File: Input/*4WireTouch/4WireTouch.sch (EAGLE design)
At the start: 15 parts, among them U2 DRV8834RGET

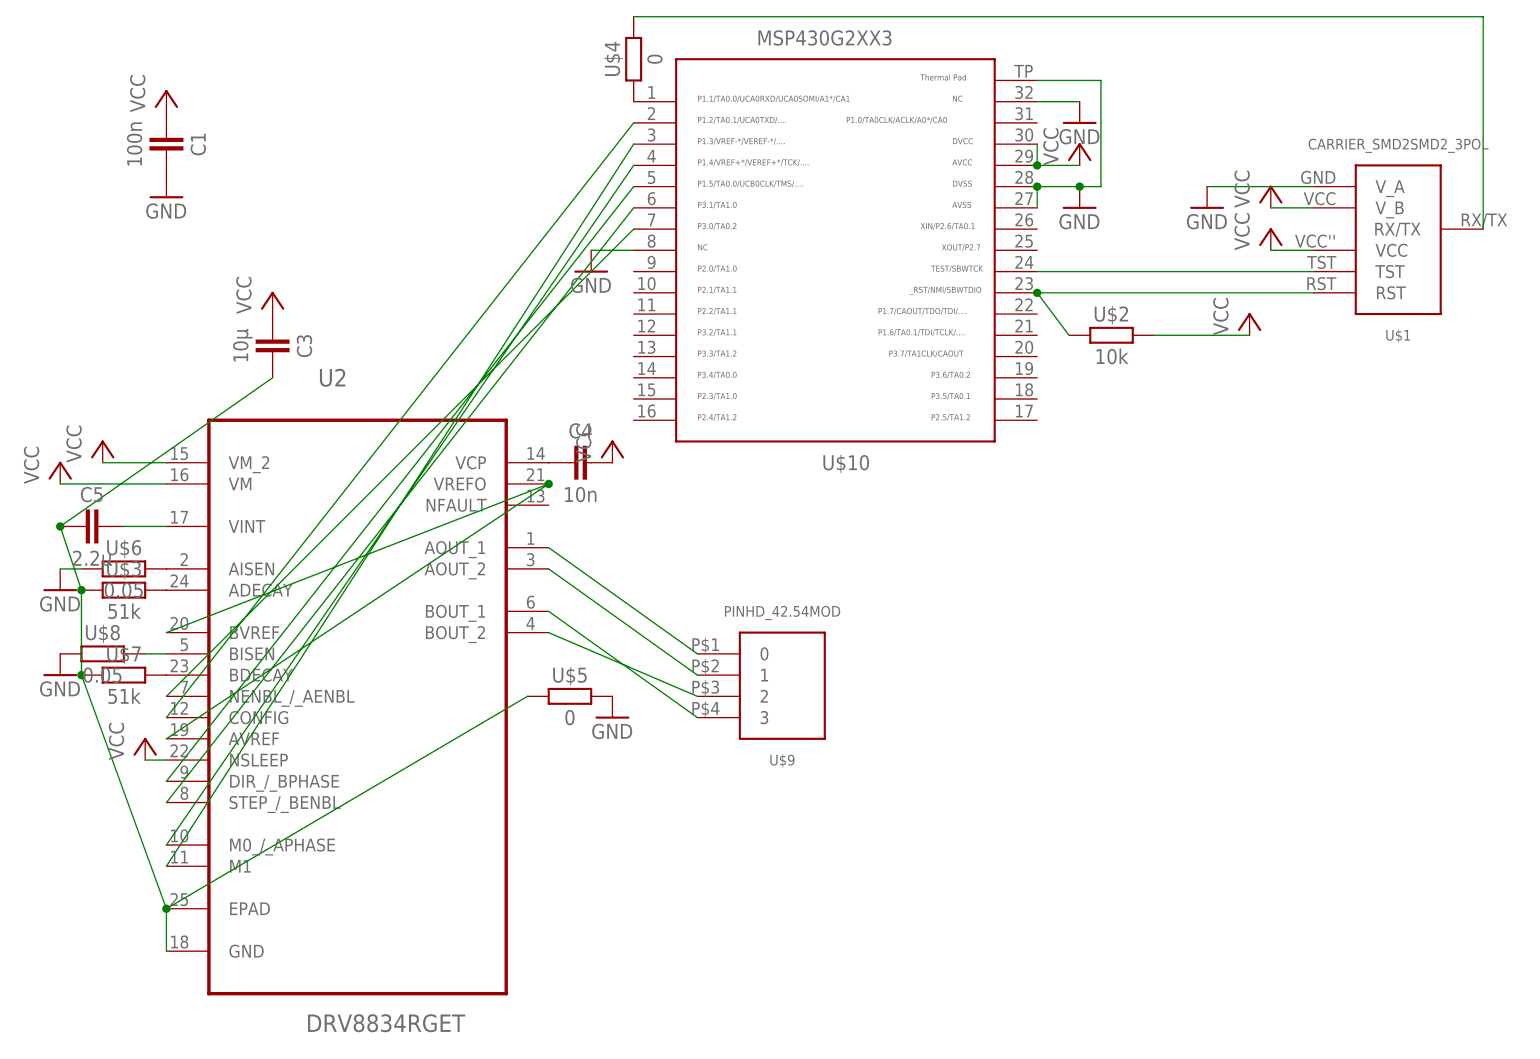
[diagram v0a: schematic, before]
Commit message: Update Pinheader
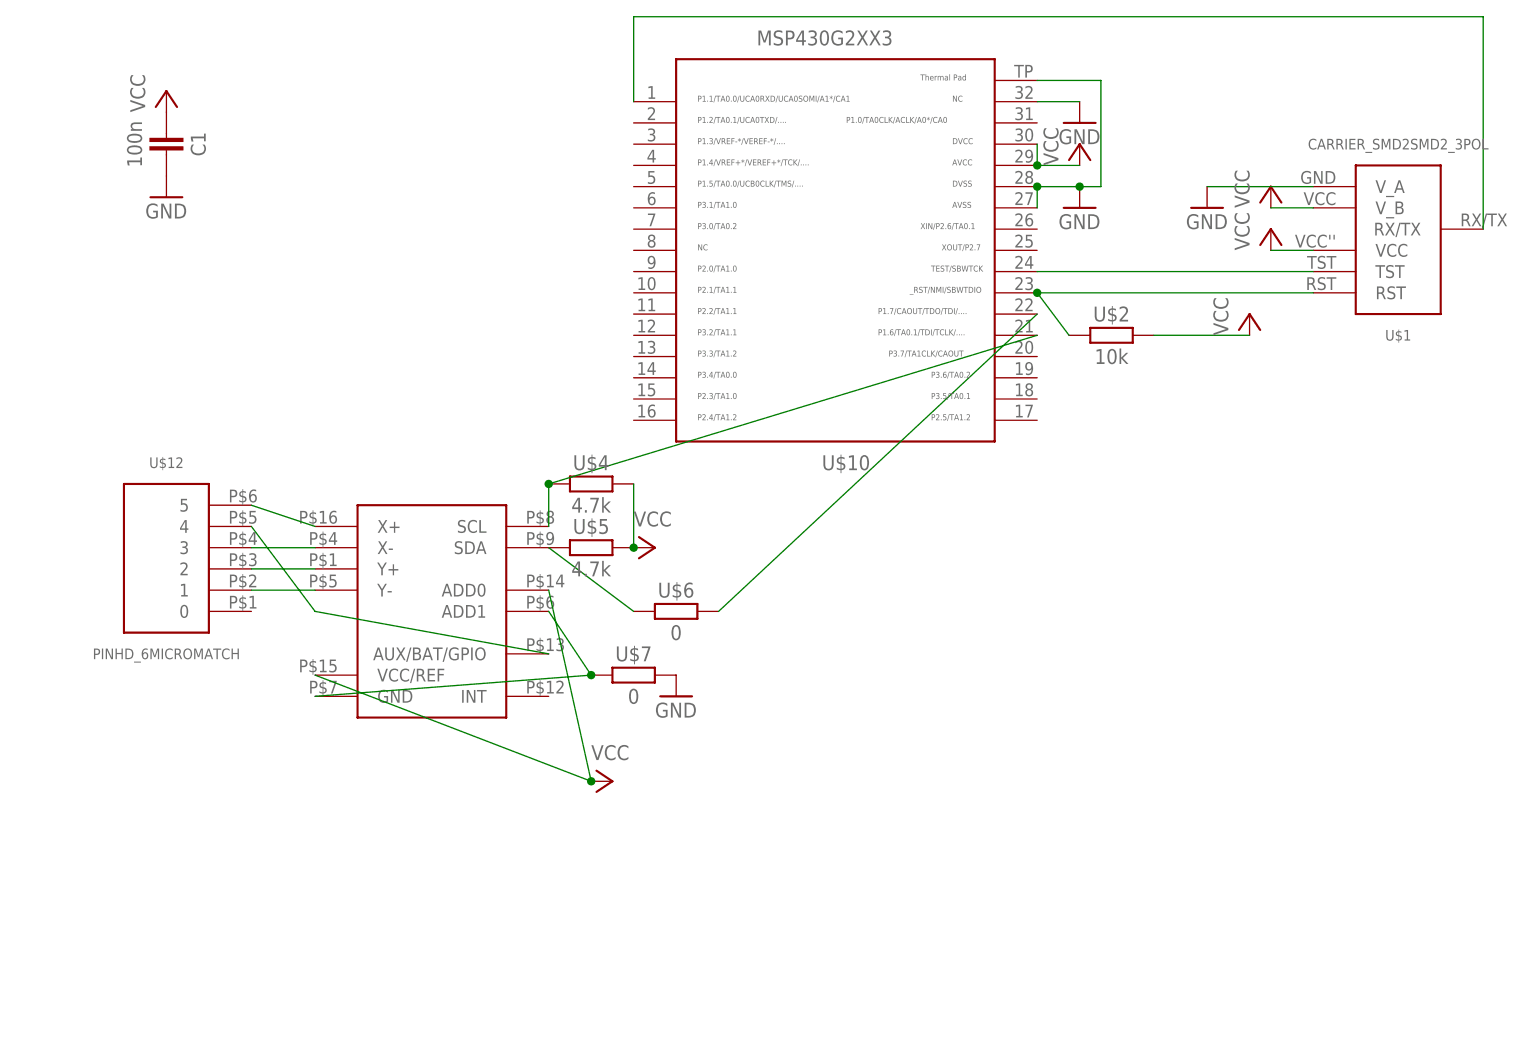
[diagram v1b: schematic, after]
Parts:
- removed C3: 10µ, thar:CAPACITOR
- removed C4: 10n, thar:CAPACITOR
- removed C5: 2.2µ, thar:CAPACITOR
- removed U$8: 0.05, thar:RESISTOR0603
- removed U$9: PINHD_42.54MOD, thar:PINHD_42.54MOD
- removed U2: DRV8834RGET, DRV8834_QFN:DRV8834RGET
- added U$12: PINHD_6MICROMATCH, thar:PINHD_6MICROMATCH
- U$3: value 51k -> AD7879; device thar:RESISTOR0603 -> thar:AD7879
- U$4, U$5: value 0 -> 4.7k
- U$6: value 0.05 -> 0
- U$7: value 51k -> 0
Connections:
- removed net N$18: U$9.2, U2.BOUT_2
- removed net N$21: C3.2, C5.1, U$3.1, U$5.1, U$7.1, U2.EPAD, U2.GND
- removed net N$23: U$9.0, U2.AOUT_1
- removed net N$24: U$9.1, U2.AOUT_2
- removed net N$27: U2.AVREF, U2.BVREF, U2.VREFO
- removed net N$29: U$10.4, U2.M0_/_APHASE
- removed net N$32: U$10.3, U2.M1
- removed net N$34: U$10.7, U2.NENBL_/_AENBL
- removed net N$35: U$10.6, U2.STEP_/_BENBL
- removed net N$36: U$10.2, U2.CONFIG
- removed net N$37: U$10.5, U2.DIR_/_BPHASE
- new net N$15: U$10.22, U$6.2
- net GND: now also U$7.2; no longer U$10.8, U$5.2, U$6.1, U$8.1
- net N$11: now also U$12.3, U$3.X-; no longer U$10.1, U$4.1
- net N$12: now also U$10.1; no longer U$4.2
- net N$13: now also U$12.2, U$3.Y+; no longer U$6.2, U2.AISEN
- net N$14: now also U$12.5, U$3.X+; no longer U$8.2, U2.BISEN
- net N$16: now also U$3.ADD1, U$3.GND, U$7.1; no longer U$9.3, U2.BOUT_1
- net N$2: now also U$10.21, U$3.SCL, U$4.1; no longer C5.2, U2.VINT
- net N$5: now also U$3.SDA, U$5.1, U$6.1; no longer C4.1, U2.VCP
- net N$6: now also U$12.4, U$3.AUX/BAT/GPIO; no longer U$3.2, U2.ADECAY
- net N$7: now also U$12.1, U$3.Y-; no longer U$7.2, U2.BDECAY
- net VCC: now also U$3.ADD0, U$3.VCC/REF, U$4.2, U$5.2; no longer C3.1, C4.2, U2.NSLEEP, U2.VM, U2.VM_2
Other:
- moved on the sheet: U$4, U$5, U$6, U$7
